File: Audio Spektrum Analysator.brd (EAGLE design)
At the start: 144.8 x 98.7 mm, 156 parts, among them IC1 LM324N, IC10 LM3914N, IC11 LM3914N, IC12 LM3914N, IC13 LM3914N, IC2 LM324N, IC3 LM324N, IC4 LM3914N, IC5 LM3914N, IC6 LM3914N, IC7 LM3914N, IC8 LM3914N, IC9 LM3914N, J2 DCJ0202, M1 ELECTRET_MICROPHON-F6050AP

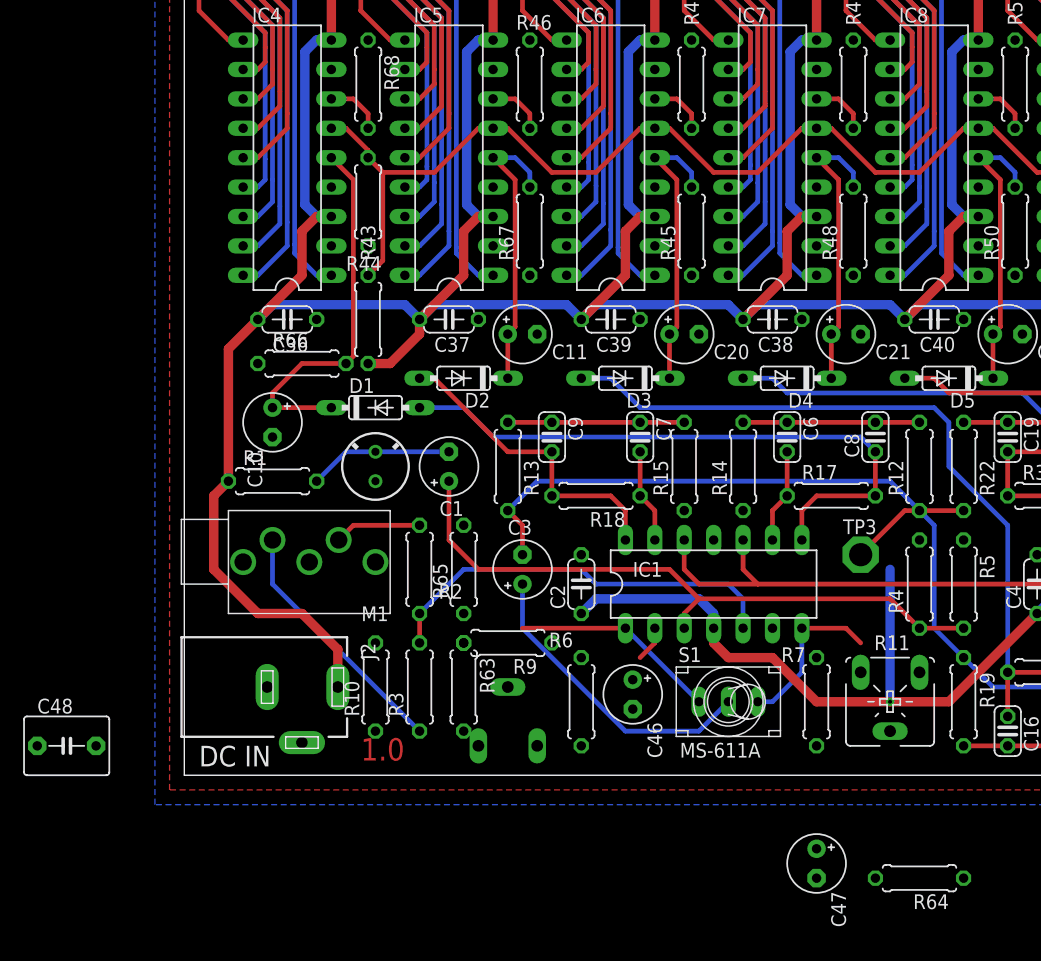
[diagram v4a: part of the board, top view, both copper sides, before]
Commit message: added RLO offest compensation in the schematic
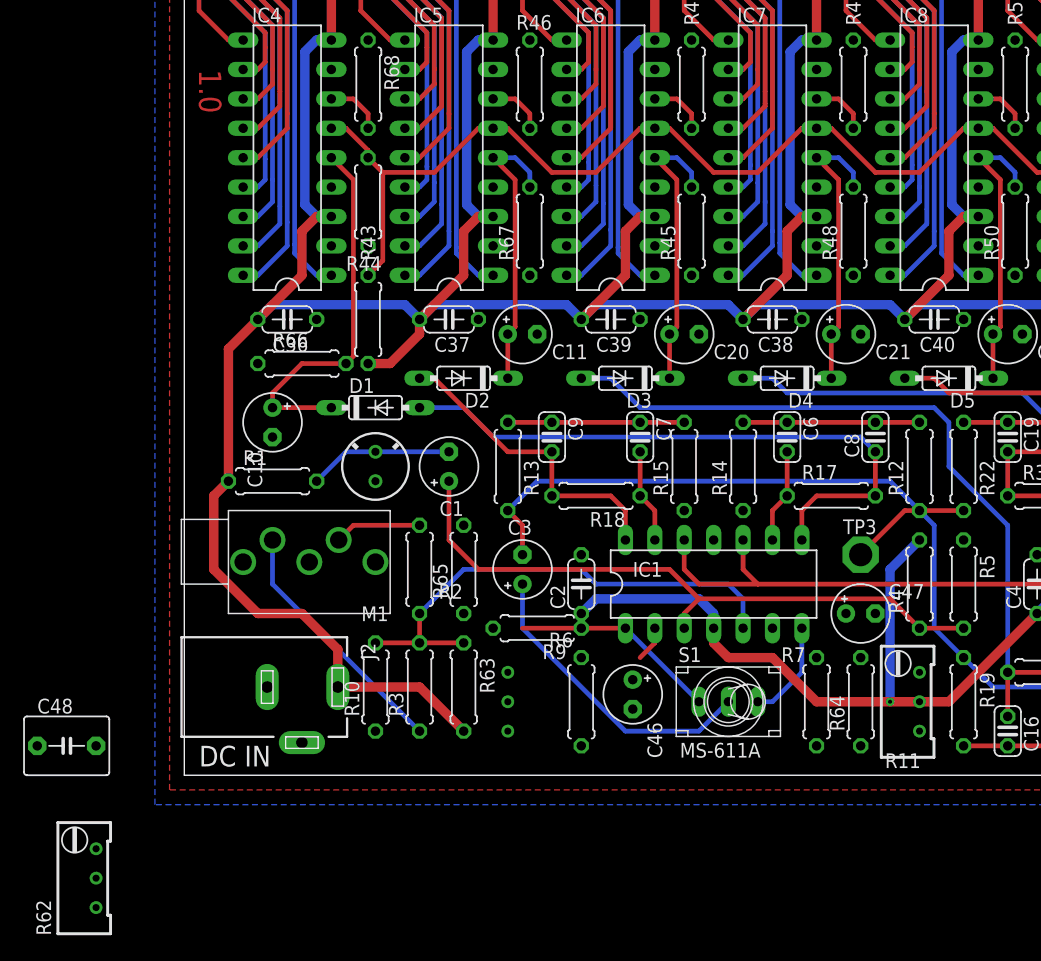
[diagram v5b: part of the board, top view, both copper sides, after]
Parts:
- added R62: 50k, resistor:RTRIM64W
- R11, R8: device pot:CA6V -> resistor:RTRIM64W
- moved C47 21.9 mm to (58.4, 14.0), turned to 0 degrees
- moved R64 16.1 mm to (58.4, 6.35), turned to 90 degrees
- moved R9 2.84 mm to (30.5, 12.7)
- moved R8 1.80 mm to (29.2, 6.35)
- moved R11 1.27 mm to (62.2, 6.35), turned to 0 degrees
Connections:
- new net RLO: IC10.4, IC11.4, IC12.4, IC13.4, IC4.4, IC5.4, IC6.4, IC7.4, IC8.4, IC9.4, R62.2
- net GND: now also R11.2, R62.1, R8.2; no longer IC10.4, IC11.4, IC12.4, IC13.4, IC4.4, IC5.4, IC6.4, IC7.4, IC8.4, IC9.4, R11.S, R8.S
- net N$44: now also R8.3; no longer R8.E
- net N$83: now also R11.3; no longer R11.E
- net V+: now also R62.3
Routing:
- net V+: track 935.5 -> 951.5 mm
- net N$3: track 35.7 -> 43.3 mm
- net N$10: track 14.3 -> 8.67 mm

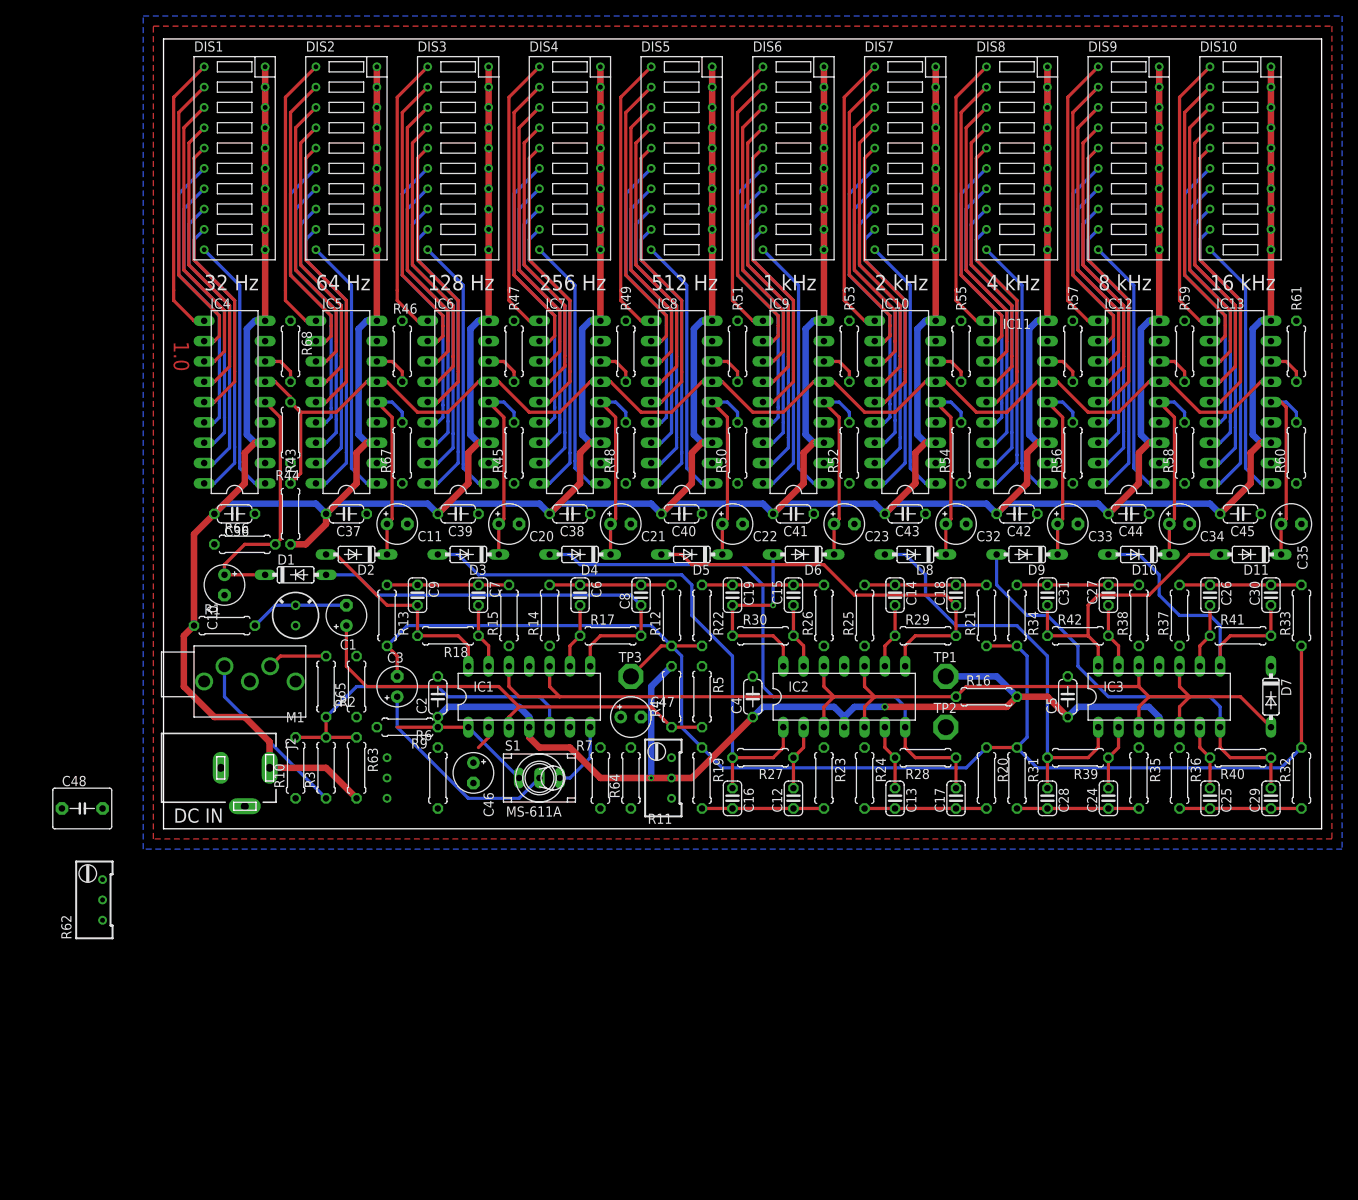
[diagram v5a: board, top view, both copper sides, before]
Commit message: implemented offset compensation circuit in layout
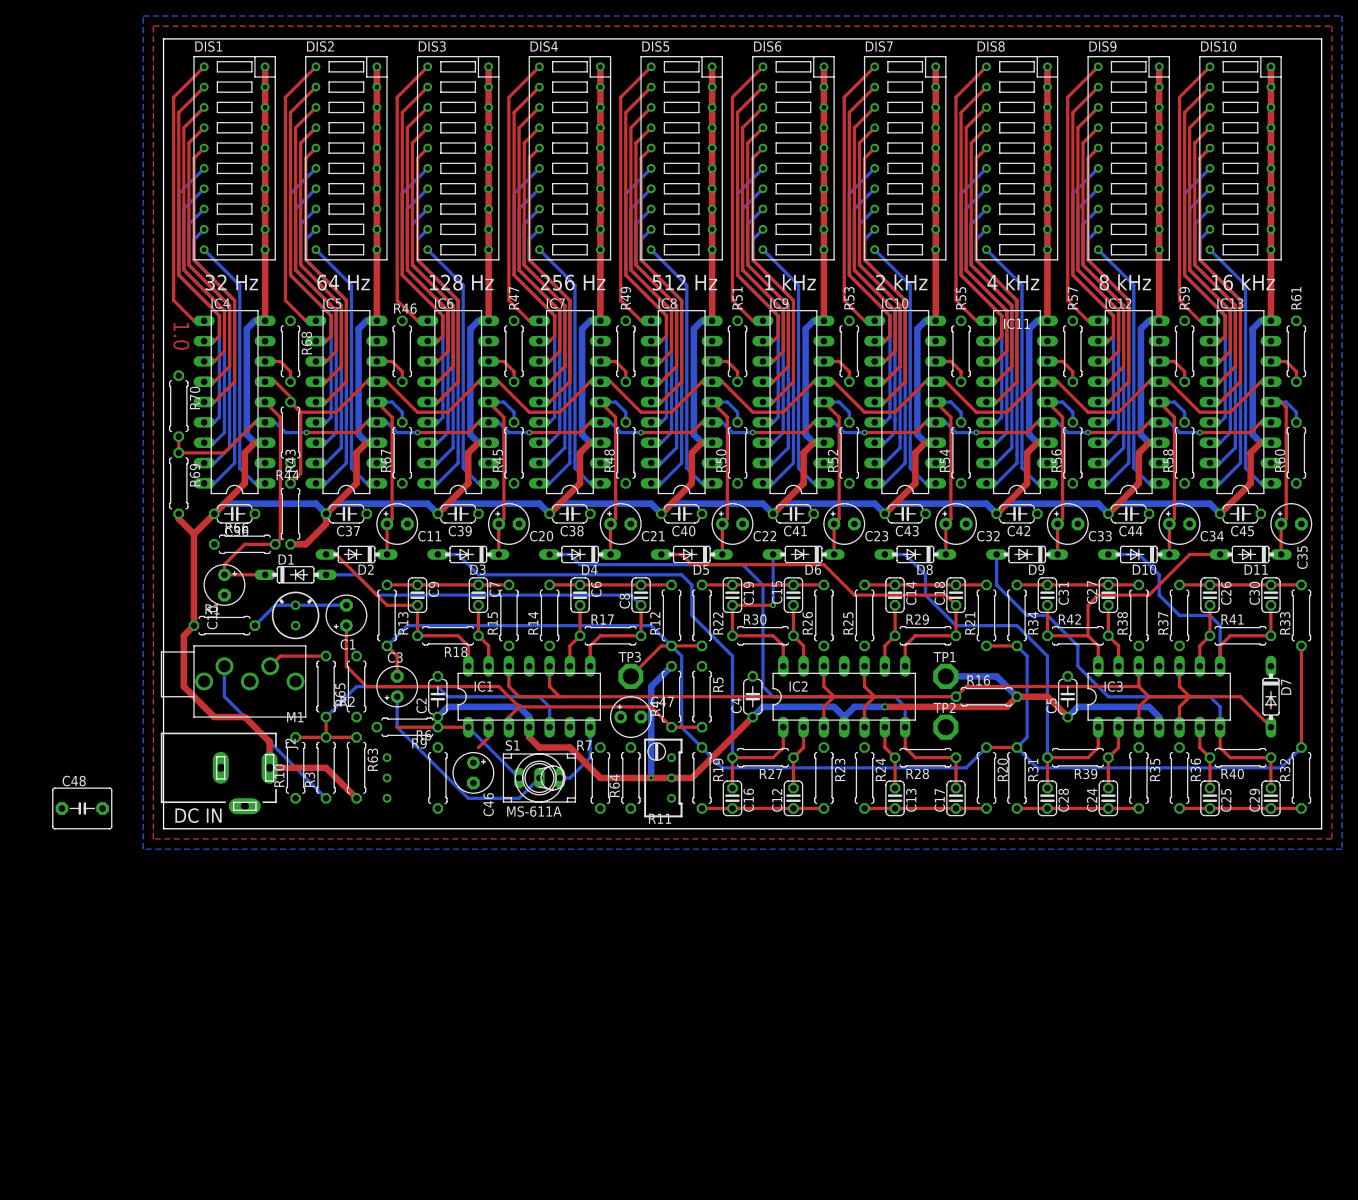
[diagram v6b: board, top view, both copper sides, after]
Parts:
- removed R62: 50k, resistor:RTRIM64W
- added R69: 9k, resistor:0207/7
- added R70: 1k, resistor:0207/7
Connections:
- net GND: now also R70.1; no longer R62.1
- net RLO: now also R69.1, R70.2; no longer R62.2
- net V+: now also R69.2; no longer R62.3
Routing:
- net RLO: track 0.00 -> 148.3 mm, vias 0 -> 9
- net V+: track 951.5 -> 954.8 mm

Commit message: swapped poti
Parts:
- flipped R8 to the top
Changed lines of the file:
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@@
 </element>
 <element name="C46" library="resistor" library_urn="urn:adsk.eagle:library:348" package="E2,5-5" package3d_urn="urn:adsk.eagle:package:23344/1" value="2u2" x="38.735" y="6.985" rot="R270"/>
-<element name="R8" library="resistor" library_urn="urn:adsk.eagle:library:348" package="RTRIM64W" package3d_urn="urn:adsk.eagle:package:23748/1" value="10k" x="29.21" y="6.35" rot="MR0"/>
+<element name="R8" library="resistor" library_urn="urn:adsk.eagle:library:348" package="RTRIM64W" package3d_urn="urn:adsk.eagle:package:23748/1" value="10k" x="29.21" y="6.35"/>
 <element name="R9" library="rcl" library_urn="urn:adsk.eagle:library:334" package="0207/7" package3d_urn="urn:adsk.eagle:package:23493/1" value="100k" x="30.48" y="12.7" rot="R180">
 <attribute name="SPICEPREFIX" value="R" x="30.48" y="12.7" size="1.778" layer="27" font="vector" rot="R180" display="off"/>
@@
 <wire x1="7.16" y1="7.62" x2="5.08" y2="18.415" width="0" layer="19" extent="1-1"/>
 <wire x1="16.51" y1="3.81" x2="7.16" y2="7.62" width="0" layer="19" extent="1-1"/>
-<wire x1="27.94" y1="6.35" x2="16.51" y2="3.81" width="0" layer="19" extent="1-1"/>
-<wire x1="24.13" y1="13.97" x2="27.94" y2="6.35" width="0" layer="19" extent="1-1"/>
+<wire x1="30.48" y1="6.35" x2="16.51" y2="3.81" width="0" layer="19" extent="1-1"/>
+<wire x1="24.13" y1="13.97" x2="30.48" y2="6.35" width="0" layer="19" extent="1-1"/>
 <wire x1="34.29" y1="19.05" x2="24.13" y2="13.97" width="0" layer="19" extent="1-1"/>
 <wire x1="43.18" y1="22.86" x2="34.29" y2="19.05" width="0" layer="19" extent="1-1"/>
@@
 <contactref element="R8" pad="3"/>
 <contactref element="R6" pad="1"/>
-<wire x1="34.29" y1="2.54" x2="27.94" y2="8.89" width="0" layer="19" extent="1-1"/>
+<wire x1="34.29" y1="2.54" x2="30.48" y2="8.89" width="0" layer="19" extent="1-1"/>
 </signal>
 <signal name="N$83">

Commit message: finished layout
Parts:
- removed C48: 1u, capacitor-wima:C5B5
- moved C2 22.9 mm to (57.1, 16.5)
- moved R9 5.39 mm to (34.3, 16.5), turned to 90 degrees
- moved C47 3.24 mm to (61.6, 14.6)
- moved TP3 3.24 mm to (61.6, 19.7)
- moved R4 2.54 mm to (66.0, 16.5)
- moved R5 2.54 mm to (69.8, 16.5)
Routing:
- net N$57: track 0.00 -> 24.6 mm, vias 0 -> 1
- net V+: track 954.8 -> 970.4 mm
- net N$83: track 0.00 -> 8.45 mm
- net N$44: track 0.00 -> 7.93 mm
- net N$5: track 3.07 -> 11.0 mm
- net N$70: track 0.00 -> 6.29 mm
- net N$31: track 0.00 -> 6.29 mm
- net N$4: track 55.8 -> 60.3 mm
- net RLO: track 148.3 -> 149.6 mm
- net N$10: track 8.67 -> 9.94 mm
- net REF: track 138.2 -> 137.2 mm
- net N$6: track 17.9 -> 18.2 mm, vias 0 -> 1
